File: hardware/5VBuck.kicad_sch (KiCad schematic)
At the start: 12 parts, among them U16 LMR51635XDDCR

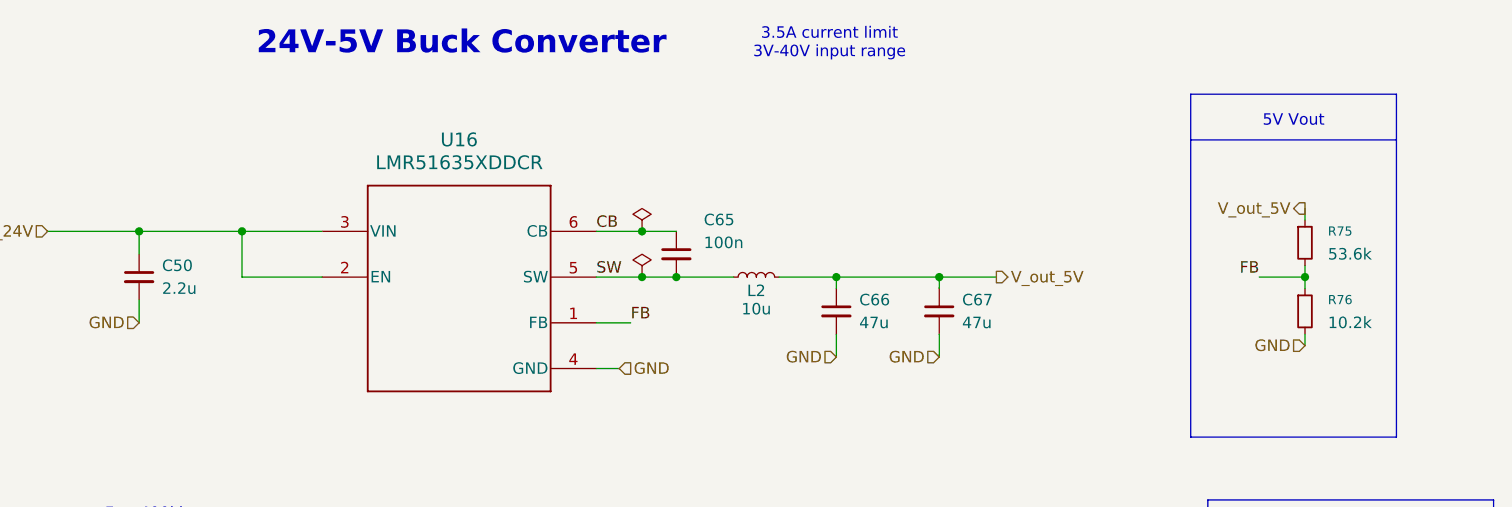
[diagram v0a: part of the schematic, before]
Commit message: fixes only thing left is finish assigning footprints, its frozen
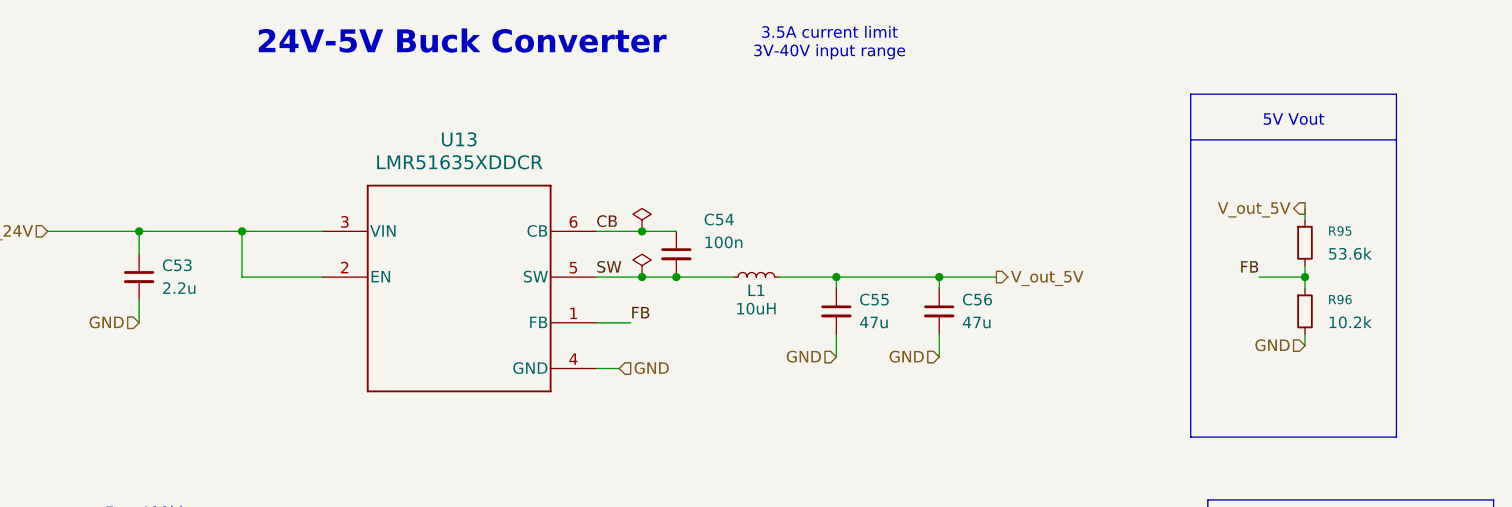
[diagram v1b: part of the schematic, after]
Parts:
- C54: renamed from C65; footprint Capacitor_SMD:C_0603_1608Metric -> Capacitor_SMD:C_0603_1608Metric_Pad1.08x0.95mm_HandSolder; Mouser P/N (none) -> MLASH168SB7104KTNA01
- L1: renamed from L2; value 10u -> 10uH
- renumbered C50 to C53, C66 to C55, C67 to C56, R75 to R95, R76 to R96, TP3 to TP19, TP4 to TP20, TP5 to TP21, TP6 to TP22, U16 to U13
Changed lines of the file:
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@@
 		(in_pos_files yes)
 		(dnp no)
-		(property "Reference" "L2"
+		(property "Reference" "L1"
 			(at 147.32 91.694 90)
 			(show_name no)
@@
 			)
 		)
-		(property "Value" "10u"
+		(property "Value" "10uH"
 			(at 147.32 93.726 90)
 			(show_name no)
@@
 			(project "PS-LVCarrier"
 				(path "/9bab2d9d-20f3-40ef-8545-e1299efec47e/194a8848-c0d2-44dd-9e5b-1946509490d6/243ac4a9-8c9a-48d2-8744-855b9f7d516f"
-					(reference "L2")
+					(reference "L1")
 					(unit 1)
 				)
@@
 		(dnp no)
 		(fields_autoplaced yes)
-		(property "Reference" "R76"
+		(property "Reference" "R96"
 			(at 210.82 92.7099 0)
 			(show_name no)
@@
 			(project "PS-LVCarrier"
 				(path "/9bab2d9d-20f3-40ef-8545-e1299efec47e/194a8848-c0d2-44dd-9e5b-1946509490d6/243ac4a9-8c9a-48d2-8744-855b9f7d516f"
-					(reference "R76")
+					(reference "R96")
 					(unit 1)
 				)
@@
 		(dnp no)
 		(fields_autoplaced yes)
-		(property "Reference" "C50"
+		(property "Reference" "C53"
 			(at 81.28 88.9062 0)
 			(show_name no)
@@
 			(project "PS-LVCarrier"
 				(path "/9bab2d9d-20f3-40ef-8545-e1299efec47e/194a8848-c0d2-44dd-9e5b-1946509490d6/243ac4a9-8c9a-48d2-8744-855b9f7d516f"
-					(reference "C50")
+					(reference "C53")
 					(unit 1)
 				)
@@
 		(in_pos_files yes)
 		(dnp no)
-		(property "Reference" "TP5"
+		(property "Reference" "TP21"
 			(at 224.79 123.6979 0)
 			(hide yes)
@@
 			(project "PS-LVCarrier"
 				(path "/9bab2d9d-20f3-40ef-8545-e1299efec47e/194a8848-c0d2-44dd-9e5b-1946509490d6/243ac4a9-8c9a-48d2-8744-855b9f7d516f"
-					(reference "TP5")
+					(reference "TP21")
 					(unit 1)
 				)
@@
 		(in_pos_files yes)
 		(dnp no)
-		(property "Reference" "C65"
+		(property "Reference" "C54"
 			(at 141.478 83.82 0)
 			(show_name no)
@@
 			)
 		)
-		(property "Footprint" "Capacitor_SMD:C_0603_1608Metric"
+		(property "Footprint" "Capacitor_SMD:C_0603_1608Metric_Pad1.08x0.95mm_HandSolder"
 			(at 138.43 87.63 0)
 			(hide yes)
@@
 		)
 		(property "LCSC P/N" "C14663"
+			(at 138.43 87.63 0)
+			(hide yes)
+			(show_name no)
+			(do_not_autoplace no)
+			(effects
+				(font
+					(size 1.27 1.27)
+				)
+			)
+		)
+		(property "Mouser P/N" "MLASH168SB7104KTNA01"
 			(at 138.43 87.63 0)
 			(hide yes)
@@
 			(project "PS-LVCarrier"
 				(path "/9bab2d9d-20f3-40ef-8545-e1299efec47e/194a8848-c0d2-44dd-9e5b-1946509490d6/243ac4a9-8c9a-48d2-8744-855b9f7d516f"
-					(reference "C65")
+					(reference "C54")
 					(unit 1)
 				)
@@
 		(dnp no)
 		(fields_autoplaced yes)
-		(property "Reference" "U16"
+		(property "Reference" "U13"
 			(at 114.3 74.93 0)
 			(show_name no)
@@
 			(project "PS-LVCarrier"
 				(path "/9bab2d9d-20f3-40ef-8545-e1299efec47e/194a8848-c0d2-44dd-9e5b-1946509490d6/243ac4a9-8c9a-48d2-8744-855b9f7d516f"
-					(reference "U16")
+					(reference "U13")
 					(unit 1)
 				)
@@
 		(in_pos_files yes)
 		(dnp no)
-		(property "Reference" "TP3"
+		(property "Reference" "TP19"
 			(at 212.09 123.6979 0)
 			(hide yes)
@@
 			(project "PS-LVCarrier"
 				(path "/9bab2d9d-20f3-40ef-8545-e1299efec47e/194a8848-c0d2-44dd-9e5b-1946509490d6/243ac4a9-8c9a-48d2-8744-855b9f7d516f"
-					(reference "TP3")
+					(reference "TP19")
 					(unit 1)
 				)
@@
 		(in_pos_files yes)
 		(dnp no)
-		(property "Reference" "TP6"
+		(property "Reference" "TP22"
 			(at 224.79 136.3979 0)
 			(hide yes)
@@
 			(project "PS-LVCarrier"
 				(path "/9bab2d9d-20f3-40ef-8545-e1299efec47e/194a8848-c0d2-44dd-9e5b-1946509490d6/243ac4a9-8c9a-48d2-8744-855b9f7d516f"
-					(reference "TP6")
+					(reference "TP22")
 					(unit 1)
 				)
@@
 		(dnp no)
 		(fields_autoplaced yes)
-		(property "Reference" "C67"
+		(property "Reference" "C56"
 			(at 170.18 92.7162 0)
 			(show_name no)
@@
 			(project "PS-LVCarrier"
 				(path "/9bab2d9d-20f3-40ef-8545-e1299efec47e/194a8848-c0d2-44dd-9e5b-1946509490d6/243ac4a9-8c9a-48d2-8744-855b9f7d516f"
-					(reference "C67")
+					(reference "C56")
 					(unit 1)
 				)
@@
 		(dnp no)
 		(fields_autoplaced yes)
-		(property "Reference" "R75"
+		(property "Reference" "R95"
 			(at 210.82 85.0899 0)
 			(show_name no)
@@
 			(project "PS-LVCarrier"
 				(path "/9bab2d9d-20f3-40ef-8545-e1299efec47e/194a8848-c0d2-44dd-9e5b-1946509490d6/243ac4a9-8c9a-48d2-8744-855b9f7d516f"
-					(reference "R75")
+					(reference "R95")
 					(unit 1)
 				)
@@
 		(dnp no)
 		(fields_autoplaced yes)
-		(property "Reference" "C66"
+		(property "Reference" "C55"
 			(at 158.75 92.7162 0)
 			(show_name no)
@@
 			(project "PS-LVCarrier"
 				(path "/9bab2d9d-20f3-40ef-8545-e1299efec47e/194a8848-c0d2-44dd-9e5b-1946509490d6/243ac4a9-8c9a-48d2-8744-855b9f7d516f"
-					(reference "C66")
+					(reference "C55")
 					(unit 1)
 				)
@@
 		(in_pos_files yes)
 		(dnp no)
-		(property "Reference" "TP4"
+		(property "Reference" "TP20"
 			(at 212.09 136.3979 0)
 			(hide yes)
@@
 			(project "PS-LVCarrier"
 				(path "/9bab2d9d-20f3-40ef-8545-e1299efec47e/194a8848-c0d2-44dd-9e5b-1946509490d6/243ac4a9-8c9a-48d2-8744-855b9f7d516f"
-					(reference "TP4")
-					(unit 1)
-				)
+					(reference "TP20")
+					(unit 1)
+				)

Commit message: switch branch
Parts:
- renumbered C53 to C61, C54 to C62, C55 to C63, C56 to C64, R95 to R100, R96 to R101, TP19 to TP23, TP20 to TP24, TP21 to TP25, TP22 to TP26
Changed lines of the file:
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@@
 		(dnp no)
 		(fields_autoplaced yes)
-		(property "Reference" "R96"
+		(property "Reference" "R101"
 			(at 210.82 92.7099 0)
 			(show_name no)
@@
 			(project "PS-LVCarrier"
 				(path "/9bab2d9d-20f3-40ef-8545-e1299efec47e/194a8848-c0d2-44dd-9e5b-1946509490d6/243ac4a9-8c9a-48d2-8744-855b9f7d516f"
-					(reference "R96")
+					(reference "R101")
 					(unit 1)
 				)
@@
 		(dnp no)
 		(fields_autoplaced yes)
-		(property "Reference" "C53"
+		(property "Reference" "C61"
 			(at 81.28 88.9062 0)
 			(show_name no)
@@
 			(project "PS-LVCarrier"
 				(path "/9bab2d9d-20f3-40ef-8545-e1299efec47e/194a8848-c0d2-44dd-9e5b-1946509490d6/243ac4a9-8c9a-48d2-8744-855b9f7d516f"
-					(reference "C53")
+					(reference "C61")
 					(unit 1)
 				)
@@
 		(in_pos_files yes)
 		(dnp no)
-		(property "Reference" "TP21"
+		(property "Reference" "TP25"
 			(at 224.79 123.6979 0)
 			(hide yes)
@@
 			(project "PS-LVCarrier"
 				(path "/9bab2d9d-20f3-40ef-8545-e1299efec47e/194a8848-c0d2-44dd-9e5b-1946509490d6/243ac4a9-8c9a-48d2-8744-855b9f7d516f"
-					(reference "TP21")
+					(reference "TP25")
 					(unit 1)
 				)
@@
 		(in_pos_files yes)
 		(dnp no)
-		(property "Reference" "C54"
+		(property "Reference" "C62"
 			(at 141.478 83.82 0)
 			(show_name no)
@@
 			(project "PS-LVCarrier"
 				(path "/9bab2d9d-20f3-40ef-8545-e1299efec47e/194a8848-c0d2-44dd-9e5b-1946509490d6/243ac4a9-8c9a-48d2-8744-855b9f7d516f"
-					(reference "C54")
+					(reference "C62")
 					(unit 1)
 				)
@@
 		(in_pos_files yes)
 		(dnp no)
-		(property "Reference" "TP19"
+		(property "Reference" "TP23"
 			(at 212.09 123.6979 0)
 			(hide yes)
@@
 			(project "PS-LVCarrier"
 				(path "/9bab2d9d-20f3-40ef-8545-e1299efec47e/194a8848-c0d2-44dd-9e5b-1946509490d6/243ac4a9-8c9a-48d2-8744-855b9f7d516f"
-					(reference "TP19")
+					(reference "TP23")
 					(unit 1)
 				)
@@
 		(dnp no)
 		(fields_autoplaced yes)
-		(property "Reference" "#FLG05"
+		(property "Reference" "#FLG04"
 			(at 134.62 83.185 0)
 			(hide yes)
@@
 			(project "PS-LVCarrier"
 				(path "/9bab2d9d-20f3-40ef-8545-e1299efec47e/194a8848-c0d2-44dd-9e5b-1946509490d6/243ac4a9-8c9a-48d2-8744-855b9f7d516f"
-					(reference "#FLG05")
+					(reference "#FLG04")
 					(unit 1)
 				)
@@
 		(in_pos_files yes)
 		(dnp no)
-		(property "Reference" "TP22"
+		(property "Reference" "TP26"
 			(at 224.79 136.3979 0)
 			(hide yes)
@@
 			(project "PS-LVCarrier"
 				(path "/9bab2d9d-20f3-40ef-8545-e1299efec47e/194a8848-c0d2-44dd-9e5b-1946509490d6/243ac4a9-8c9a-48d2-8744-855b9f7d516f"
-					(reference "TP22")
+					(reference "TP26")
 					(unit 1)
 				)
@@
 		(dnp no)
 		(fields_autoplaced yes)
-		(property "Reference" "C56"
+		(property "Reference" "C64"
 			(at 170.18 92.7162 0)
 			(show_name no)
@@
 			(project "PS-LVCarrier"
 				(path "/9bab2d9d-20f3-40ef-8545-e1299efec47e/194a8848-c0d2-44dd-9e5b-1946509490d6/243ac4a9-8c9a-48d2-8744-855b9f7d516f"
-					(reference "C56")
+					(reference "C64")
 					(unit 1)
 				)
@@
 		(in_pos_files yes)
 		(dnp no)
-		(property "Reference" "#FLG06"
+		(property "Reference" "#FLG05"
 			(at 134.62 88.265 0)
 			(hide yes)
@@
 			(project "PS-LVCarrier"
 				(path "/9bab2d9d-20f3-40ef-8545-e1299efec47e/194a8848-c0d2-44dd-9e5b-1946509490d6/243ac4a9-8c9a-48d2-8744-855b9f7d516f"
-					(reference "#FLG06")
+					(reference "#FLG05")
 					(unit 1)
 				)
@@
 		(dnp no)
 		(fields_autoplaced yes)
-		(property "Reference" "R95"
+		(property "Reference" "R100"
 			(at 210.82 85.0899 0)
 			(show_name no)
@@
 			(project "PS-LVCarrier"
 				(path "/9bab2d9d-20f3-40ef-8545-e1299efec47e/194a8848-c0d2-44dd-9e5b-1946509490d6/243ac4a9-8c9a-48d2-8744-855b9f7d516f"
-					(reference "R95")
+					(reference "R100")
 					(unit 1)
 				)
@@
 		(dnp no)
 		(fields_autoplaced yes)
-		(property "Reference" "C55"
+		(property "Reference" "C63"
 			(at 158.75 92.7162 0)
 			(show_name no)
@@
 			(project "PS-LVCarrier"
 				(path "/9bab2d9d-20f3-40ef-8545-e1299efec47e/194a8848-c0d2-44dd-9e5b-1946509490d6/243ac4a9-8c9a-48d2-8744-855b9f7d516f"
-					(reference "C55")
+					(reference "C63")
 					(unit 1)
 				)
@@
 		(in_pos_files yes)
 		(dnp no)
-		(property "Reference" "TP20"
+		(property "Reference" "TP24"
 			(at 212.09 136.3979 0)
 			(hide yes)
@@
 			(project "PS-LVCarrier"
 				(path "/9bab2d9d-20f3-40ef-8545-e1299efec47e/194a8848-c0d2-44dd-9e5b-1946509490d6/243ac4a9-8c9a-48d2-8744-855b9f7d516f"
-					(reference "TP20")
-					(unit 1)
-				)
+					(reference "TP24")
+					(unit 1)
+				)

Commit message: review ts
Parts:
- renumbered C61 to C47, C62 to C48, C63 to C49, C64 to C50, R100 to R51, R101 to R52, TP23 to TP28, TP24 to TP29, TP25 to TP30, TP26 to TP31, U13 to U10
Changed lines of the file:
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@@
 		(dnp no)
 		(fields_autoplaced yes)
-		(property "Reference" "R101"
+		(property "Reference" "R52"
 			(at 210.82 92.7099 0)
 			(show_name no)
@@
 			(project "PS-LVCarrier"
 				(path "/9bab2d9d-20f3-40ef-8545-e1299efec47e/194a8848-c0d2-44dd-9e5b-1946509490d6/243ac4a9-8c9a-48d2-8744-855b9f7d516f"
-					(reference "R101")
+					(reference "R52")
 					(unit 1)
 				)
@@
 		(dnp no)
 		(fields_autoplaced yes)
-		(property "Reference" "C61"
+		(property "Reference" "C47"
 			(at 81.28 88.9062 0)
 			(show_name no)
@@
 			(project "PS-LVCarrier"
 				(path "/9bab2d9d-20f3-40ef-8545-e1299efec47e/194a8848-c0d2-44dd-9e5b-1946509490d6/243ac4a9-8c9a-48d2-8744-855b9f7d516f"
-					(reference "C61")
+					(reference "C47")
 					(unit 1)
 				)
@@
 		(in_pos_files yes)
 		(dnp no)
-		(property "Reference" "TP25"
+		(property "Reference" "TP30"
 			(at 224.79 123.6979 0)
 			(hide yes)
@@
 			(project "PS-LVCarrier"
 				(path "/9bab2d9d-20f3-40ef-8545-e1299efec47e/194a8848-c0d2-44dd-9e5b-1946509490d6/243ac4a9-8c9a-48d2-8744-855b9f7d516f"
-					(reference "TP25")
+					(reference "TP30")
 					(unit 1)
 				)
@@
 		(in_pos_files yes)
 		(dnp no)
-		(property "Reference" "C62"
+		(property "Reference" "C48"
 			(at 141.478 83.82 0)
 			(show_name no)
@@
 			(project "PS-LVCarrier"
 				(path "/9bab2d9d-20f3-40ef-8545-e1299efec47e/194a8848-c0d2-44dd-9e5b-1946509490d6/243ac4a9-8c9a-48d2-8744-855b9f7d516f"
-					(reference "C62")
+					(reference "C48")
 					(unit 1)
 				)
@@
 		(dnp no)
 		(fields_autoplaced yes)
-		(property "Reference" "U13"
+		(property "Reference" "U10"
 			(at 114.3 74.93 0)
 			(show_name no)
@@
 			(project "PS-LVCarrier"
 				(path "/9bab2d9d-20f3-40ef-8545-e1299efec47e/194a8848-c0d2-44dd-9e5b-1946509490d6/243ac4a9-8c9a-48d2-8744-855b9f7d516f"
-					(reference "U13")
+					(reference "U10")
 					(unit 1)
 				)
@@
 		(in_pos_files yes)
 		(dnp no)
-		(property "Reference" "TP23"
+		(property "Reference" "TP28"
 			(at 212.09 123.6979 0)
 			(hide yes)
@@
 			(project "PS-LVCarrier"
 				(path "/9bab2d9d-20f3-40ef-8545-e1299efec47e/194a8848-c0d2-44dd-9e5b-1946509490d6/243ac4a9-8c9a-48d2-8744-855b9f7d516f"
-					(reference "TP23")
+					(reference "TP28")
 					(unit 1)
 				)
@@
 		(dnp no)
 		(fields_autoplaced yes)
-		(property "Reference" "#FLG04"
+		(property "Reference" "#FLG03"
 			(at 134.62 83.185 0)
 			(hide yes)
@@
 			(project "PS-LVCarrier"
 				(path "/9bab2d9d-20f3-40ef-8545-e1299efec47e/194a8848-c0d2-44dd-9e5b-1946509490d6/243ac4a9-8c9a-48d2-8744-855b9f7d516f"
-					(reference "#FLG04")
+					(reference "#FLG03")
 					(unit 1)
 				)
@@
 		(in_pos_files yes)
 		(dnp no)
-		(property "Reference" "TP26"
+		(property "Reference" "TP31"
 			(at 224.79 136.3979 0)
 			(hide yes)
@@
 			(project "PS-LVCarrier"
 				(path "/9bab2d9d-20f3-40ef-8545-e1299efec47e/194a8848-c0d2-44dd-9e5b-1946509490d6/243ac4a9-8c9a-48d2-8744-855b9f7d516f"
-					(reference "TP26")
+					(reference "TP31")
 					(unit 1)
 				)
@@
 		(dnp no)
 		(fields_autoplaced yes)
-		(property "Reference" "C64"
+		(property "Reference" "C50"
 			(at 170.18 92.7162 0)
 			(show_name no)
@@
 			(project "PS-LVCarrier"
 				(path "/9bab2d9d-20f3-40ef-8545-e1299efec47e/194a8848-c0d2-44dd-9e5b-1946509490d6/243ac4a9-8c9a-48d2-8744-855b9f7d516f"
-					(reference "C64")
+					(reference "C50")
 					(unit 1)
 				)
@@
 		(in_pos_files yes)
 		(dnp no)
-		(property "Reference" "#FLG05"
+		(property "Reference" "#FLG04"
 			(at 134.62 88.265 0)
 			(hide yes)
@@
 			(project "PS-LVCarrier"
 				(path "/9bab2d9d-20f3-40ef-8545-e1299efec47e/194a8848-c0d2-44dd-9e5b-1946509490d6/243ac4a9-8c9a-48d2-8744-855b9f7d516f"
-					(reference "#FLG05")
+					(reference "#FLG04")
 					(unit 1)
 				)
@@
 		(dnp no)
 		(fields_autoplaced yes)
-		(property "Reference" "R100"
+		(property "Reference" "R51"
 			(at 210.82 85.0899 0)
 			(show_name no)
@@
 			(project "PS-LVCarrier"
 				(path "/9bab2d9d-20f3-40ef-8545-e1299efec47e/194a8848-c0d2-44dd-9e5b-1946509490d6/243ac4a9-8c9a-48d2-8744-855b9f7d516f"
-					(reference "R100")
+					(reference "R51")
 					(unit 1)
 				)
@@
 		(dnp no)
 		(fields_autoplaced yes)
-		(property "Reference" "C63"
+		(property "Reference" "C49"
 			(at 158.75 92.7162 0)
 			(show_name no)
@@
 			(project "PS-LVCarrier"
 				(path "/9bab2d9d-20f3-40ef-8545-e1299efec47e/194a8848-c0d2-44dd-9e5b-1946509490d6/243ac4a9-8c9a-48d2-8744-855b9f7d516f"
-					(reference "C63")
+					(reference "C49")
 					(unit 1)
 				)
@@
 		(in_pos_files yes)
 		(dnp no)
-		(property "Reference" "TP24"
+		(property "Reference" "TP29"
 			(at 212.09 136.3979 0)
 			(hide yes)
@@
 			(project "PS-LVCarrier"
 				(path "/9bab2d9d-20f3-40ef-8545-e1299efec47e/194a8848-c0d2-44dd-9e5b-1946509490d6/243ac4a9-8c9a-48d2-8744-855b9f7d516f"
-					(reference "TP24")
-					(unit 1)
-				)
+					(reference "TP29")
+					(unit 1)
+				)

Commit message: addressed
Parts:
- removed TP28: V_in_24V, TestPoint:TestPoint_THTPad_D3.0mm_Drill1.5mm, symbol Connector:TestPoint
- removed TP29: CB, TestPoint:TestPoint_THTPad_D3.0mm_Drill1.5mm, symbol Connector:TestPoint
- removed TP30: FB, TestPoint:TestPoint_THTPad_D3.0mm_Drill1.5mm, symbol Connector:TestPoint
- removed TP31: SW, TestPoint:TestPoint_THTPad_D3.0mm_Drill1.5mm, symbol Connector:TestPoint
- added TP18: V_in_12V, TestPoint:TestPoint_THTPad_D3.0mm_Drill1.5mm, symbol Connector:TestPoint
- added TP19: CB, TestPoint:TestPoint_THTPad_D3.0mm_Drill1.5mm, symbol Connector:TestPoint
- added TP20: FB, TestPoint:TestPoint_THTPad_D3.0mm_Drill1.5mm, symbol Connector:TestPoint
- added TP21: SW, TestPoint:TestPoint_THTPad_D3.0mm_Drill1.5mm, symbol Connector:TestPoint
- C47: value 2.2u -> 4.7u; LCSC P/N C1771 -> (none); P/N CL21F225ZAFNNNE -> MSASL168SB5475KTNA01
- C48: footprint Capacitor_SMD:C_0603_1608Metric_Pad1.08x0.95mm_HandSolder -> Capacitor_SMD:C_0805_2012Metric_Pad1.18x1.45mm_HandSolder; LCSC P/N C14663 -> (none); Mouser P/N MLASH168SB7104KTNA01 -> (none)
- C49: value 47u -> 100n; footprint Capacitor_SMD:C_1210_3225Metric_Pad1.33x2.70mm_HandSolder -> Capacitor_SMD:C_0603_1608Metric; LCSC P/N C77101 -> (none); P/N GRM32ER61C476KE15L -> MLASH168SB7104KTNA01
- C50: LCSC P/N C77101 -> (none); P/N GRM32ER61C476KE15L -> ZRB18AC80E476ME01L
- L1: value 10uH -> 8.2u; footprint LHRS_Passives:SRN8040-101M -> LHRS_Passives:SRN8040-150M; LCSC P/N C54563397 -> (none); P/N SRN8040-101M -> 74439369082
- R51: value 53.6k -> 100k; LCSC P/N C23074 -> (none); P/N 0603WAF5362T5E -> AE1206BR-07100KL
- R52: value 10.2k -> 19.1k; LCSC P/N C22772 -> (none); P/N 0603WAF1022T5E -> ERA-2ARB1912X
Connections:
- net CB: now also C49.1, TP19.1; no longer C48.1
- net FB: now also TP20.1
- net GND: now also C48.2; no longer C49.2
- net SW: now also C49.2, TP21.1; no longer C48.2
- net V_out_5V: no longer C49.1
- net V_in_24V renamed V_in_12V
- net V_in_12V: now also C48.1, TP18.1
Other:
- note added: "12V Vout"
- note added: "12V-5V Buck Converter"
- note added: "Vout 5"
- note removed: "24V-5V Buck Converter"
- note removed: "5V Vout"
